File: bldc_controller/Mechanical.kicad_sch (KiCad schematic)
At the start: 0 parts

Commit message: added temporary footprints and deleted extra files
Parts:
- added C108: 330n, Capacitor_SMD:C_0402_1005Metric, symbol Device:C_Small
- added H1, H3: M3, MountingHole:MountingHole_3.2mm_M3_Pad_Via, symbol Mechanical:MountingHole
- added H2: M3, MountingHole:MountingHole_3.2mm_M3_Pad_Via, symbol Mechanical:MountingHole_Pad
- added R45: 100k, Resistor_SMD:R_0402_1005Metric, symbol Device:R_Small
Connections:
- new net: C108.1, H2.1, R45.1
- new net -VBAT: C108.2, R45.2
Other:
- company: (none) -> EPFL Xplore
- title: (none) -> Mechanical Parts
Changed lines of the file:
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@@
 (kicad_sch (version 20230121) (generator eeschema)
   (paper "A4")
+  (title_block
+    (title "Mechanical Parts")
+    (date "2023-10-22")
+    (rev "1.0")
+    (company "EPFL Xplore")
+    (comment 3 "Author: Vincent Nguyen")
+  )
+  (junction (at 146.05 86.36) (diameter 0) (color 0 0 0 0)
+  )
+  (junction (at 146.05 97.79) (diameter 0) (color 0 0 0 0)
+  )
+  (polyline (pts (xy 111.76 73.66) (xy 111.76 116.84))
+    (stroke (width 0) (type default))
+  )
+  (wire (pts (xy 146.05 83.82) (xy 146.05 86.36))
+    (stroke (width 0) (type default))
+  )
+  (wire (pts (xy 140.97 86.36) (xy 140.97 88.9))
+    (stroke (width 0) (type default))
+  )
+  (polyline (pts (xy 184.15 73.66) (xy 184.15 116.84))
+    (stroke (width 0) (type default))
+  )
+  (wire (pts (xy 146.05 97.79) (xy 151.13 97.79))
+    (stroke (width 0) (type default))
+  )
+  (wire (pts (xy 146.05 86.36) (xy 140.97 86.36))
+    (stroke (width 0) (type default))
+  )
+  (wire (pts (xy 151.13 97.79) (xy 151.13 93.98))
+    (stroke (width 0) (type default))
+  )
+  (wire (pts (xy 140.97 93.98) (xy 140.97 97.79))
+    (stroke (width 0) (type default))
+  )
+  (wire (pts (xy 140.97 97.79) (xy 146.05 97.79))
+    (stroke (width 0) (type default))
+  )
+  (wire (pts (xy 151.13 86.36) (xy 146.05 86.36))
+    (stroke (width 0) (type default))
+  )
+  (wire (pts (xy 146.05 97.79) (xy 146.05 101.6))
+    (stroke (width 0) (type default))
+  )
+  (polyline (pts (xy 115.57 69.85) (xy 180.34 69.85))
+    (stroke (width 0) (type default))
+  )
+  (polyline (pts (xy 180.34 120.65) (xy 115.57 120.65))
+    (stroke (width 0) (type default))
+  )
+  (wire (pts (xy 151.13 88.9) (xy 151.13 86.36))
+    (stroke (width 0) (type default))
+  )
+  (arc (start 184.15 116.84) (mid 183.037 119.537) (end 180.34 120.65)
+    (stroke (width 0) (type default))
+    (fill (type none))
+  )
+  (arc (start 111.76 73.66) (mid 112.8759 70.9659) (end 115.57 69.85)
+    (stroke (width 0) (type default))
+    (fill (type none))
+  )
+  (arc (start 180.34 69.85) (mid 183.0341 70.9659) (end 184.15 73.66)
+    (stroke (width 0) (type default))
+    (fill (type none))
+  )
+  (arc (start 115.57 120.65) (mid 112.8759 119.5341) (end 111.76 116.84)
+    (stroke (width 0) (type default))
+    (fill (type none))
+  )
+  (text_box "Optional RC filter for chassis grounding."
+    (at 151.13 99.06 0) (size 24.13 6.35)
+    (stroke (width 0) (type default))
+    (fill (type color) (color 191 240 255 1))
+    (effects (font (size 1.27 1.27) (color 0 0 0 1)) (justify left top))
+  )
+  (text_box "Mounting holes"
+    (at 114.3 109.22 0) (size 66.675 9.525)
+    (stroke (width -0.0001) (type default))
+    (fill (type none))
+    (effects (font (size 2.54 2.54) (thickness 0.508) bold (color 0 0 0 1)) (justify bottom))
+  )
+  (text_box "Back to Top Level"
+    (at 265.43 166.37 0) (size 19.05 14.605)
+    (stroke (width 0) (type default) (color 0 0 0 1))
+    (fill (type color) (color 0 0 0 0.1))
+    (effects (font (size 2.54 2.54) (thickness 0.508) bold (color 0 0 0 1)) (href "#1"))
+  )
+  (symbol (lib_id "0_power_symbols:-VBAT") (at 146.05 101.6 180) (unit 1)
+    (in_bom yes) (on_board yes) (dnp no) (fields_autoplaced)
+    (property "Reference" "#PWR073" (at 146.05 104.14 0)
+      (effects (font (size 1.27 1.27)) hide)
+    )
+    (property "Value" "-VBAT" (at 146.05 106.68 0)
+      (effects (font (size 1.27 1.27)))
+    )
+    (property "Footprint" "" (at 146.05 101.6 0)
+      (effects (font (size 1.27 1.27)) hide)
+    )
+    (property "Datasheet" "" (at 146.05 101.6 0)
+      (effects (font (size 1.27 1.27)) hide)
+    )
+    (pin "1")
+    (instances
+      (project "bldc_controller"
+        (path "/0650c7a8-acba-429c-9f8e-eec0baf0bc1c/f1a92623-4681-4556-bc2b-558e74890d89"
+          (reference "#PWR073") (unit 1)
+        )
+      )
+    )
+  )
+  (symbol (lib_id "Mechanical:MountingHole") (at 124.46 80.01 0) (unit 1)
+    (in_bom yes) (on_board yes) (dnp no) (fields_autoplaced)
+    (property "Reference" "H1" (at 127 78.74 0)
+      (effects (font (size 1.27 1.27)) (justify left))
+    )
+    (property "Value" "M3" (at 127 81.28 0)
+      (effects (font (size 1.27 1.27)) (justify left))
+    )
+    (property "Footprint" "MountingHole:MountingHole_3.2mm_M3_Pad_Via" (at 124.46 80.01 0)
+      (effects (font (size 1.27 1.27)) hide)
+    )
+    (property "Datasheet" "~" (at 124.46 80.01 0)
+      (effects (font (size 1.27 1.27)) hide)
+    )
+    (instances
+      (project "bldc_controller"
+        (path "/0650c7a8-acba-429c-9f8e-eec0baf0bc1c/f1a92623-4681-4556-bc2b-558e74890d89"
+          (reference "H1") (unit 1)
+        )
+      )
+    )
+  )
+  (symbol (lib_id "Device:R_Small") (at 151.13 91.44 0) (unit 1)
+    (in_bom yes) (on_board yes) (dnp yes) (fields_autoplaced)
+    (property "Reference" "R45" (at 153.67 90.17 0)
+      (effects (font (size 1.27 1.27)) (justify left))
+    )
+    (property "Value" "100k" (at 153.67 92.71 0)
+      (effects (font (size 1.27 1.27)) (justify left))
+    )
+    (property "Footprint" "Resistor_SMD:R_0402_1005Metric" (at 151.13 91.44 0)
+      (effects (font (size 1.27 1.27)) hide)
+    )
+    (property "Datasheet" "~" (at 151.13 91.44 0)
+      (effects (font (size 1.27 1.27)) hide)
+    )
+    (pin "1")
+    (pin "2")
+    (instances
+      (project "bldc_controller"
+        (path "/0650c7a8-acba-429c-9f8e-eec0baf0bc1c/f1a92623-4681-4556-bc2b-558e74890d89"
+          (reference "R45") (unit 1)
+        )
+      )
+    )
+  )
+  (symbol (lib_id "Device:C_Small") (at 140.97 91.44 0) (unit 1)
+    (in_bom no) (on_board yes) (dnp yes) (fields_autoplaced)
+    (property "Reference" "C108" (at 143.51 90.1763 0)
+      (effects (font (size 1.27 1.27)) (justify left))
+    )
+    (property "Value" "330n" (at 143.51 92.7163 0)
+      (effects (font (size 1.27 1.27)) (justify left))
+    )
+    (property "Footprint" "Capacitor_SMD:C_0402_1005Metric" (at 140.97 91.44 0)
+      (effects (font (size 1.27 1.27)) hide)
+    )
+    (property "Datasheet" "~" (at 140.97 91.44 0)
+      (effects (font (size 1.27 1.27)) hide)
+    )
+    (pin "1")
+    (pin "2")
+    (instances
+      (project "bldc_controller"
+        (path "/0650c7a8-acba-429c-9f8e-eec0baf0bc1c/f1a92623-4681-4556-bc2b-558e74890d89"
+          (reference "C108") (unit 1)
+        )
+      )
+    )
+  )
+  (symbol (lib_id "Mechanical:MountingHole") (at 167.64 80.01 0) (unit 1)
+    (in_bom yes) (on_board yes) (dnp no) (fields_autoplaced)
+    (property "Reference" "H3" (at 170.18 78.74 0)
+      (effects (font (size 1.27 1.27)) (justify left))
+    )
+    (property "Value" "M3" (at 170.18 81.28 0)
+      (effects (font (size 1.27 1.27)) (justify left))
+    )
+    (property "Footprint" "MountingHole:MountingHole_3.2mm_M3_Pad_Via" (at 167.64 80.01 0)
+      (effects (font (size 1.27 1.27)) hide)
+    )
+    (property "Datasheet" "~" (at 167.64 80.01 0)
+      (effects (font (size 1.27 1.27)) hide)
+    )
+    (instances
+      (project "bldc_controller"
+        (path "/0650c7a8-acba-429c-9f8e-eec0baf0bc1c/f1a92623-4681-4556-bc2b-558e74890d89"
+          (reference "H3") (unit 1)
+        )
+      )
+    )
+  )
+  (symbol (lib_id "Mechanical:MountingHole_Pad") (at 146.05 81.28 0) (unit 1)
+    (in_bom yes) (on_board yes) (dnp no) (fields_autoplaced)
+    (property "Reference" "H2" (at 148.59 78.74 0)
+      (effects (font (size 1.27 1.27)) (justify left))
+    )
+    (property "Value" "M3" (at 148.59 81.28 0)
+      (effects (font (size 1.27 1.27)) (justify left))
+    )
+    (property "Footprint" "MountingHole:MountingHole_3.2mm_M3_Pad_Via" (at 146.05 81.28 0)
+      (effects (font (size 1.27 1.27)) hide)
+    )
+    (property "Datasheet" "~" (at 146.05 81.28 0)
+      (effects (font (size 1.27 1.27)) hide)
+    )
+    (pin "1")
+    (instances
+      (project "bldc_controller"
+        (path "/0650c7a8-acba-429c-9f8e-eec0baf0bc1c/f1a92623-4681-4556-bc2b-558e74890d89"
+          (reference "H2") (unit 1)
+        )
+      )
+    )
+  )
 )

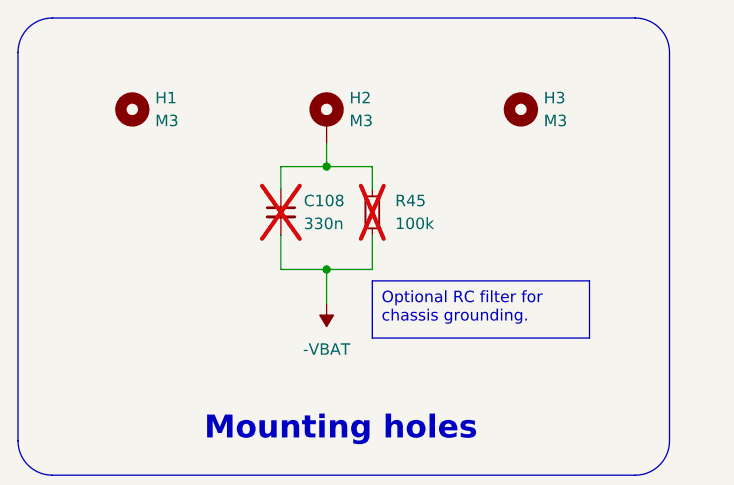
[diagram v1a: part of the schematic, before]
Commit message: added IPC-7351 compliant footprints and started routing
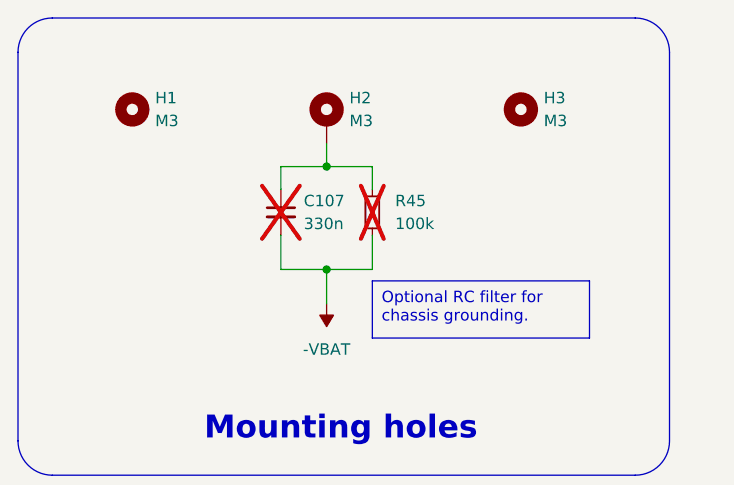
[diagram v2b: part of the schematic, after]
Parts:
- C107: renamed from C108; footprint Capacitor_SMD:C_0402_1005Metric -> 0_capacitor_smd:C_0402_1005_DensityHigh
- R45: footprint Resistor_SMD:R_0402_1005Metric -> 0_resistor_smd:R_0402_1005_DensityHigh
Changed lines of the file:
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@@
   (symbol (lib_id "0_power_symbols:-VBAT") (at 146.05 101.6 180) (unit 1)
     (in_bom yes) (on_board yes) (dnp no) (fields_autoplaced)
-    (property "Reference" "#PWR073" (at 146.05 104.14 0)
+    (property "Reference" "#PWR072" (at 146.05 104.14 0)
       (effects (font (size 1.27 1.27)) hide)
     )
@@
       (project "bldc_controller"
         (path "/0650c7a8-acba-429c-9f8e-eec0baf0bc1c/f1a92623-4681-4556-bc2b-558e74890d89"
-          (reference "#PWR073") (unit 1)
+          (reference "#PWR072") (unit 1)
         )
       )
@@
       (effects (font (size 1.27 1.27)) (justify left))
     )
-    (property "Footprint" "Resistor_SMD:R_0402_1005Metric" (at 151.13 91.44 0)
+    (property "Footprint" "0_resistor_smd:R_0402_1005_DensityHigh" (at 151.13 91.44 0)
       (effects (font (size 1.27 1.27)) hide)
     )
@@
   (symbol (lib_id "Device:C_Small") (at 140.97 91.44 0) (unit 1)
     (in_bom no) (on_board yes) (dnp yes) (fields_autoplaced)
-    (property "Reference" "C108" (at 143.51 90.1763 0)
+    (property "Reference" "C107" (at 143.51 90.1763 0)
       (effects (font (size 1.27 1.27)) (justify left))
     )
@@
       (effects (font (size 1.27 1.27)) (justify left))
     )
-    (property "Footprint" "Capacitor_SMD:C_0402_1005Metric" (at 140.97 91.44 0)
+    (property "Footprint" "0_capacitor_smd:C_0402_1005_DensityHigh" (at 140.97 91.44 0)
       (effects (font (size 1.27 1.27)) hide)
     )
@@
       (project "bldc_controller"
         (path "/0650c7a8-acba-429c-9f8e-eec0baf0bc1c/f1a92623-4681-4556-bc2b-558e74890d89"
-          (reference "C108") (unit 1)
+          (reference "C107") (unit 1)
         )
       )

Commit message: some progress on the pcb
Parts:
- removed H1, H3: M3, MountingHole:MountingHole_3.2mm_M3_Pad_Via, symbol Mechanical:MountingHole
- added H1, H3: M3, 0_pad:MountingHole_3.2mm_M3_Pad_Via, symbol Mechanical:MountingHole_Pad
- H2: footprint MountingHole:MountingHole_3.2mm_M3_Pad_Via -> 0_pad:MountingHole_3.2mm_M3_Pad_Via
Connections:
- net CHASSIS: now reaches C107.1, H2.1, R45.1
- net CHASSIS: now also H1.1, H3.1
- net -VBAT renamed GND
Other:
- moved on the sheet: C107, R45

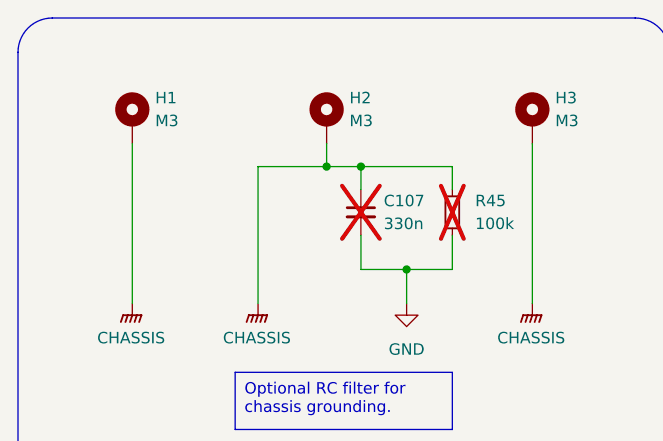
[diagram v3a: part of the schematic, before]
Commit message: added 12V buck
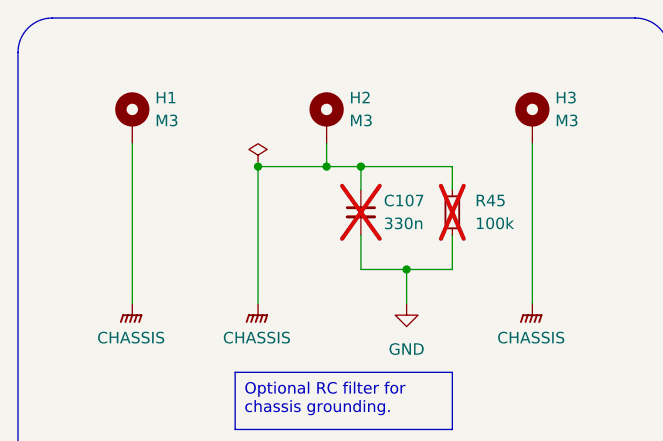
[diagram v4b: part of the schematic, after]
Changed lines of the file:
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@@
     (comment 3 "Author: Vincent Nguyen")
+  )
+  (junction (at 138.43 86.36) (diameter 0) (color 0 0 0 0)
   )
   (junction (at 146.05 86.36) (diameter 0) (color 0 0 0 0)
@@
         )
       )
+    )
+  )
+  (symbol (lib_id "power:PWR_FLAG") (at 138.43 86.36 0) (unit 1)
+    (in_bom yes) (on_board yes) (dnp no) (fields_autoplaced)
+    (property "Reference" "#FLG01" (at 138.43 84.455 0)
+      (effects (font (size 1.27 1.27)) hide)
+    )
+    (property "Value" "PWR_FLAG" (at 138.43 81.28 0)
+      (effects (font (size 1.27 1.27)) hide)
+    )
+    (property "Footprint" "" (at 138.43 86.36 0)
+      (effects (font (size 1.27 1.27)) hide)
+    )
+    (property "Datasheet" "~" (at 138.43 86.36 0)
+      (effects (font (size 1.27 1.27)) hide)
+    )
+    (pin "1")
+    (instances
+      (project "bldc_controller"
+        (path "/0650c7a8-acba-429c-9f8e-eec0baf0bc1c"
+          (reference "#FLG01") (unit 1)
+        )
+        (path "/0650c7a8-acba-429c-9f8e-eec0baf0bc1c/f1a92623-4681-4556-bc2b-558e74890d89"
+          (reference "#FLG08") (unit 1)
+        )
+      )

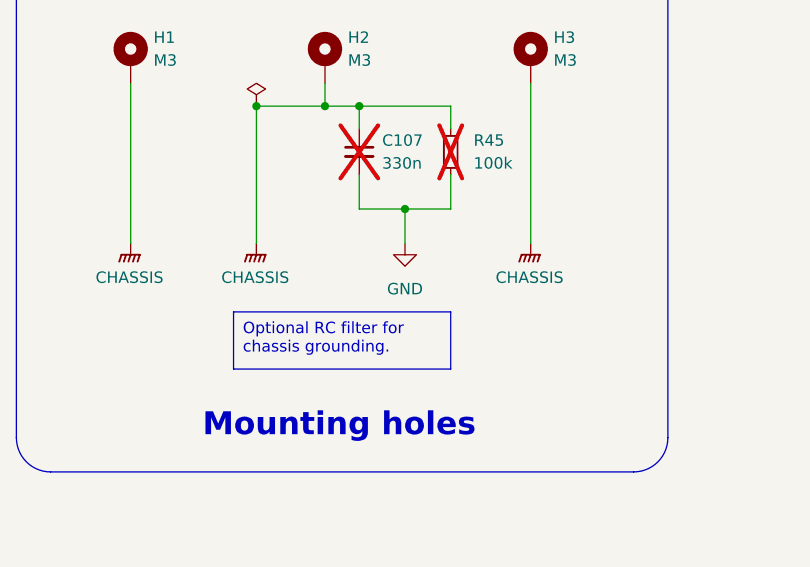
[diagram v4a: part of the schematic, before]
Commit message: added power domains. Risk of ground shift near CAN
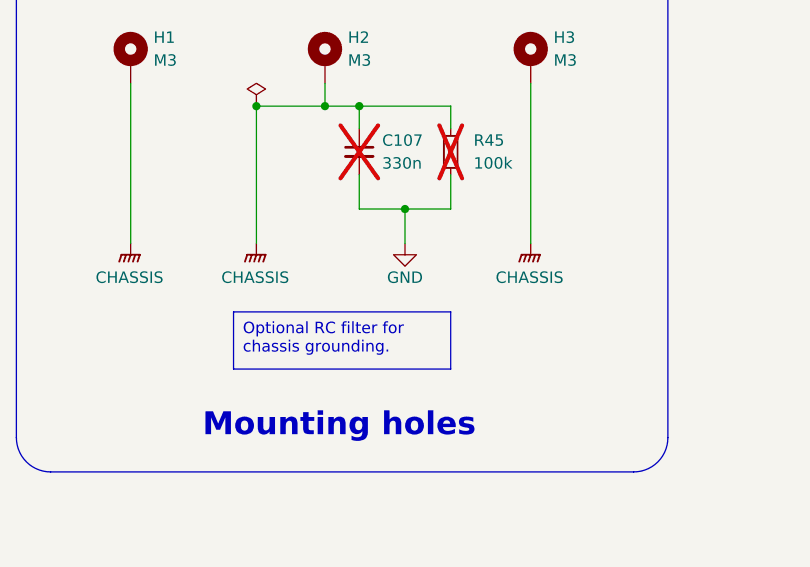
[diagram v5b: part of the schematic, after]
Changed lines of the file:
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@@
     (comment 3 "Author: Vincent Nguyen")
   )
-  (junction (at 138.43 86.36) (diameter 0) (color 0 0 0 0)
-  )
-  (junction (at 146.05 86.36) (diameter 0) (color 0 0 0 0)
-  )
-  (junction (at 154.94 97.79) (diameter 0) (color 0 0 0 0)
-  )
-  (junction (at 149.86 86.36) (diameter 0) (color 0 0 0 0)
+  (junction (at 138.43 86.36) (diameter 0) (color 139 103 213 1)
+  )
+  (junction (at 146.05 86.36) (diameter 0) (color 139 103 213 1)
+  )
+  (junction (at 154.94 97.79) (diameter 0) (color 0 0 0 1)
+  )
+  (junction (at 149.86 86.36) (diameter 0) (color 139 103 213 1)
   )
   (polyline (pts (xy 111.76 73.66) (xy 111.76 123.19))
@@
   )
   (wire (pts (xy 146.05 83.82) (xy 146.05 86.36))
-    (stroke (width 0) (type default))
+    (stroke (width 0) (type default) (color 139 103 213 1))
   )
   (wire (pts (xy 149.86 86.36) (xy 149.86 88.9))
-    (stroke (width 0) (type default))
+    (stroke (width 0) (type default) (color 139 103 213 1))
   )
   (polyline (pts (xy 184.15 73.66) (xy 184.15 123.19))
@@
   )
   (wire (pts (xy 154.94 97.79) (xy 160.02 97.79))
-    (stroke (width 0) (type default))
+    (stroke (width 0) (type default) (color 0 0 0 1))
   )
   (wire (pts (xy 160.02 97.79) (xy 160.02 93.98))
-    (stroke (width 0) (type default))
+    (stroke (width 0) (type default) (color 0 0 0 1))
   )
   (wire (pts (xy 149.86 93.98) (xy 149.86 97.79))
-    (stroke (width 0) (type default))
+    (stroke (width 0) (type default) (color 0 0 0 1))
   )
   (wire (pts (xy 124.46 101.6) (xy 124.46 83.82))
-    (stroke (width 0) (type default))
+    (stroke (width 0) (type default) (color 139 103 213 1))
   )
   (wire (pts (xy 149.86 97.79) (xy 154.94 97.79))
-    (stroke (width 0) (type default))
+    (stroke (width 0) (type default) (color 0 0 0 1))
   )
   (wire (pts (xy 160.02 86.36) (xy 149.86 86.36))
-    (stroke (width 0) (type default))
+    (stroke (width 0) (type default) (color 139 103 213 1))
   )
   (wire (pts (xy 138.43 101.6) (xy 138.43 86.36))
-    (stroke (width 0) (type default))
+    (stroke (width 0) (type default) (color 139 103 213 1))
   )
   (wire (pts (xy 149.86 86.36) (xy 146.05 86.36))
-    (stroke (width 0) (type default))
+    (stroke (width 0) (type default) (color 139 103 213 1))
   )
   (wire (pts (xy 154.94 97.79) (xy 154.94 101.6))
-    (stroke (width 0) (type default))
+    (stroke (width 0) (type default) (color 0 0 0 1))
   )
   (polyline (pts (xy 115.57 69.85) (xy 180.34 69.85))
@@
   )
   (wire (pts (xy 168.91 101.6) (xy 168.91 83.82))
-    (stroke (width 0) (type default))
+    (stroke (width 0) (type default) (color 139 103 213 1))
   )
   (wire (pts (xy 138.43 86.36) (xy 146.05 86.36))
-    (stroke (width 0) (type default))
+    (stroke (width 0) (type default) (color 139 103 213 1))
   )
   (polyline (pts (xy 180.34 127) (xy 115.57 127))
@@
   )
   (wire (pts (xy 160.02 88.9) (xy 160.02 86.36))
-    (stroke (width 0) (type default))
+    (stroke (width 0) (type default) (color 139 103 213 1))
   )
   (arc (start 184.15 123.19) (mid 183.037 125.887) (end 180.34 127)
@@
   )
   (symbol (lib_id "power:GND") (at 154.94 101.6 0) (unit 1)
-    (in_bom yes) (on_board yes) (dnp no) (fields_autoplaced)
+    (in_bom yes) (on_board yes) (dnp no)
     (property "Reference" "#PWR072" (at 154.94 107.95 0)
       (effects (font (size 1.27 1.27)) hide)
     )
-    (property "Value" "GND" (at 154.94 106.68 0)
+    (property "Value" "GND" (at 154.94 105.41 0)
       (effects (font (size 1.27 1.27)))
     )

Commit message: might have fixed net issue, added dxf and svgs
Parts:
- added C121, C122: 330n, 0_capacitor_smd:C_0402_1005_DensityHigh, symbol Device:C_Small
- added R49, R50: 100k, 0_resistor_smd:R_0402_1005_DensityHigh, symbol Device:R_Small
- C107, R45: now fitted
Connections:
- net CHASSIS: now also C121.1, C122.1, R49.1, R50.1
- net GND: now also C121.2, C122.2, R49.2, R50.2
